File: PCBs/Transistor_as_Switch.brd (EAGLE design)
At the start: 24.2 x 19 mm, 7 parts, among them T1 2N3904

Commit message: Updated
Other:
- board size 24.2 x 19 mm -> 30 x 20 mm
- board text added: "PinwheelRobotics"
- board text added: "care@pinwheel.in"
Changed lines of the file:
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@@
 <drawing>
 <settings>
-<setting alwaysvectorfont="yes"/>
+<setting alwaysvectorfont="no"/>
 <setting verticaltext="up"/>
 </settings>
-<grid distance="50" unitdist="mil" unit="mm" style="lines" multiple="1" display="yes" altdistance="5" altunitdist="mil" altunit="mm"/>
+<grid distance="0.5" unitdist="mm" unit="mm" style="lines" multiple="1" display="yes" altdistance="5" altunitdist="mil" altunit="mm"/>
 <layers>
 <layer number="1" name="Top" color="4" fill="1" visible="yes" active="yes"/>
@@
 <layer number="43" name="vRestrict" color="2" fill="10" visible="yes" active="yes"/>
 <layer number="44" name="Drills" color="7" fill="1" visible="no" active="yes"/>
-<layer number="45" name="Holes" color="7" fill="1" visible="no" active="yes"/>
+<layer number="45" name="Holes" color="7" fill="1" visible="yes" active="yes"/>
 <layer number="46" name="Milling" color="3" fill="1" visible="no" active="yes"/>
 <layer number="47" name="Measures" color="7" fill="1" visible="no" active="yes"/>
@@
 <board>
 <plain>
-<wire x1="0" y1="17.77" x2="0" y2="1.27" width="0" layer="20"/>
-<wire x1="0" y1="1.27" x2="1.27" y2="0" width="0" layer="20" curve="90"/>
-<wire x1="1.27" y1="0" x2="22.86" y2="0" width="0" layer="20"/>
-<wire x1="22.86" y1="0" x2="24.181" y2="1.321" width="0" layer="20" curve="90"/>
-<wire x1="24.181" y1="1.321" x2="24.181" y2="17.719" width="0" layer="20"/>
-<wire x1="24.181" y1="17.719" x2="22.86" y2="19.04" width="0" layer="20" curve="90"/>
-<wire x1="22.86" y1="19.04" x2="1.27" y2="19.04" width="0" layer="20"/>
-<wire x1="1.27" y1="19.04" x2="0" y2="17.77" width="0" layer="20" curve="90"/>
+<wire x1="24.612559375" y1="20" x2="-1.0266875" y2="20" width="0.1524" layer="20"/>
+<wire x1="-1.0266875" y1="20" x2="-3" y2="18.0266875" width="0.1524" layer="20" curve="90"/>
+<wire x1="-3" y1="18.0266875" x2="-3" y2="1.197415625" width="0.1524" layer="20"/>
+<wire x1="-3" y1="1.197415625" x2="-1.802584375" y2="0" width="0.1524" layer="20" curve="90"/>
+<wire x1="-1.802584375" y1="0" x2="25.654259375" y2="0" width="0.1524" layer="20"/>
+<wire x1="25.654259375" y1="0" x2="27" y2="1.345740625" width="0.1524" layer="20" curve="90"/>
+<wire x1="27" y1="1.345740625" x2="27" y2="17.612559375" width="0.1524" layer="20"/>
+<wire x1="27" y1="17.612559375" x2="24.612559375" y2="20" width="0.1524" layer="20" curve="90"/>
+<hole x="-0.889" y="17.907" drill="3"/>
+<hole x="24.992" y="17.357" drill="3"/>
+<hole x="24.992" y="1.992" drill="3"/>
+<hole x="-0.984" y="2.119" drill="3"/>
+<text x="4.191" y="18.288" size="1.4224" layer="21">PinwheelRobotics</text>
+<text x="5.461" y="11.811" size="1.27" layer="22" rot="MR180">care@pinwheel.in</text>
 </plain>
 <attributes>

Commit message: New Update
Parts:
- moved INPUT 0.52 mm to (19.3, 7.11)
- moved OUTPUT 0.28 mm to (11.8, 7.11)
- moved GND 0.18 mm to (4.32, 7.11)
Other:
- board size 30 x 20 mm -> 29.5 x 20 mm
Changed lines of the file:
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@@
 <drawing>
 <settings>
-<setting alwaysvectorfont="no"/>
+<setting alwaysvectorfont="yes"/>
 <setting verticaltext="up"/>
 </settings>
@@
 <board>
 <plain>
-<wire x1="24.612559375" y1="20" x2="-1.0266875" y2="20" width="0.1524" layer="20"/>
+<wire x1="-1.0266875" y1="20" x2="24.792896875" y2="20" width="0.1524" layer="20"/>
+<wire x1="24.792896875" y1="20" x2="26.5" y2="18.292896875" width="0.1524" layer="20" curve="-90"/>
+<wire x1="26.5" y1="18.292896875" x2="26.5" y2="0.845740625" width="0.1524" layer="20"/>
+<wire x1="26.5" y1="0.845740625" x2="25.654259375" y2="0" width="0.1524" layer="20" curve="-90"/>
 <wire x1="-1.0266875" y1="20" x2="-3" y2="18.0266875" width="0.1524" layer="20" curve="90"/>
 <wire x1="-3" y1="18.0266875" x2="-3" y2="1.197415625" width="0.1524" layer="20"/>
 <wire x1="-3" y1="1.197415625" x2="-1.802584375" y2="0" width="0.1524" layer="20" curve="90"/>
-<wire x1="-1.802584375" y1="0" x2="25.654259375" y2="0" width="0.1524" layer="20"/>
-<wire x1="25.654259375" y1="0" x2="27" y2="1.345740625" width="0.1524" layer="20" curve="90"/>
-<wire x1="27" y1="1.345740625" x2="27" y2="17.612559375" width="0.1524" layer="20"/>
-<wire x1="27" y1="17.612559375" x2="24.612559375" y2="20" width="0.1524" layer="20" curve="90"/>
-<hole x="-0.889" y="17.907" drill="3"/>
-<hole x="24.992" y="17.357" drill="3"/>
-<hole x="24.992" y="1.992" drill="3"/>
-<hole x="-0.984" y="2.119" drill="3"/>
+<wire x1="-1.802584375" y1="0" x2="25.5" y2="0" width="0.1524" layer="20"/>
+<hole x="-1" y="17.5" drill="3"/>
+<hole x="24.5" y="17.5" drill="3"/>
+<hole x="24.5" y="2" drill="3"/>
+<hole x="-1" y="2" drill="3"/>
 <text x="4.191" y="18.288" size="1.4224" layer="21">PinwheelRobotics</text>
 <text x="5.461" y="11.811" size="1.27" layer="22" rot="MR180">care@pinwheel.in</text>
+<wire x1="25.5" y1="0" x2="25.654259375" y2="0" width="0.1524" layer="20"/>
 </plain>
 <attributes>
@@
 </autorouter>
 <elements>
-<element name="GND" library="microbit" package="MICROBIT_PAD" value="MICROBIT_PAD" x="4.445" y="6.985" smashed="yes">
-<attribute name="NAME" x="2.794" y="10.414" size="0.6096" layer="21" font="vector"/>
-</element>
-<element name="INPUT" library="microbit" package="MICROBIT_PAD" value="MICROBIT_PAD" x="19.812" y="6.985" smashed="yes">
-<attribute name="NAME" x="17.399" y="10.033" size="0.6096" layer="21" font="vector"/>
+<element name="GND" library="microbit" package="MICROBIT_PAD" value="MICROBIT_PAD" x="4.318" y="7.112" smashed="yes">
+<attribute name="NAME" x="2.667" y="10.541" size="0.6096" layer="21" font="vector"/>
+</element>
+<element name="INPUT" library="microbit" package="MICROBIT_PAD" value="MICROBIT_PAD" x="19.304" y="7.112" smashed="yes">
+<attribute name="NAME" x="16.891" y="10.16" size="0.6096" layer="21" font="vector"/>
 </element>
 <element name="LED1" library="led" library_urn="urn:adsk.eagle:library:259" package="CHIP-LED0805" package3d_urn="urn:adsk.eagle:package:15818/2" value="" x="8.255" y="16.637" smashed="yes" rot="R90">
@@
 <attribute name="VALUE" x="9.525" y="19.177" size="1.27" layer="27" rot="R180"/>
 </element>
-<element name="OUTPUT" library="microbit" package="MICROBIT_PAD" value="MICROBIT_PAD" x="12.065" y="6.985" smashed="yes">
-<attribute name="NAME" x="8.89" y="10.414" size="0.6096" layer="21" font="vector"/>
+<element name="OUTPUT" library="microbit" package="MICROBIT_PAD" value="MICROBIT_PAD" x="11.811" y="7.112" smashed="yes">
+<attribute name="NAME" x="8.636" y="10.541" size="0.6096" layer="21" font="vector"/>
 </element>
 <element name="R1" library="we-rcl" package="R0207/10" value="" x="16.002" y="13.335" smashed="yes" rot="R180">
@@
 <wire x1="21.0693" y1="13.335" x2="21.002" y2="13.335" width="0.381" layer="1"/>
 <wire x1="21.0693" y1="16.5354" x2="21.002" y2="16.637" width="0.381" layer="1"/>
-<wire x1="20.8026" y1="8.001" x2="20.8026" y2="13.335" width="0.381" layer="1"/>
-<wire x1="20.0025" y1="7.2009" x2="20.8026" y2="8.001" width="0.381" layer="1"/>
+<wire x1="20.8026" y1="8.43429375" x2="20.8026" y2="13.335" width="0.381" layer="1"/>
 <wire x1="20.8026" y1="13.335" x2="21.002" y2="13.335" width="0.381" layer="1"/>
-<wire x1="20.0025" y1="7.2009" x2="19.812" y2="6.985" width="0.381" layer="1"/>
+<wire x1="20.8026" y1="8.43429375" x2="19.304" y2="7.112" width="0.381" layer="1"/>
 </signal>
 <signal name="N$1">
@@
 <wire x1="4.0005" y1="14.1351" x2="3.81" y2="13.97" width="0.381" layer="1"/>
 <wire x1="5.334" y1="13.8684" x2="4.0005" y2="13.8684" width="0.381" layer="1"/>
-<wire x1="12.0015" y1="7.2009" x2="5.334" y2="13.8684" width="0.381" layer="1"/>
+<wire x1="11.694584375" y1="7.507815625" x2="5.334" y2="13.8684" width="0.381" layer="1"/>
 <wire x1="4.0005" y1="13.8684" x2="3.81" y2="13.97" width="0.381" layer="1"/>
-<wire x1="12.0015" y1="7.2009" x2="12.065" y2="6.985" width="0.381" layer="1"/>
+<wire x1="11.694584375" y1="7.507815625" x2="11.811" y2="7.112" width="0.381" layer="1"/>
 </signal>
 <signal name="GND">
@@
 <wire x1="4.5339" y1="7.2009" x2="5.0673" y2="7.7343" width="0.381" layer="16"/>
 <wire x1="4.0005" y1="16.2687" x2="3.81" y2="16.51" width="0.381" layer="16"/>
-<wire x1="4.5339" y1="7.2009" x2="4.445" y2="6.985" width="0.381" layer="16"/>
+<wire x1="4.5339" y1="7.2009" x2="4.318" y2="7.112" width="0.381" layer="16"/>
 </signal>
 <signal name="N$3">

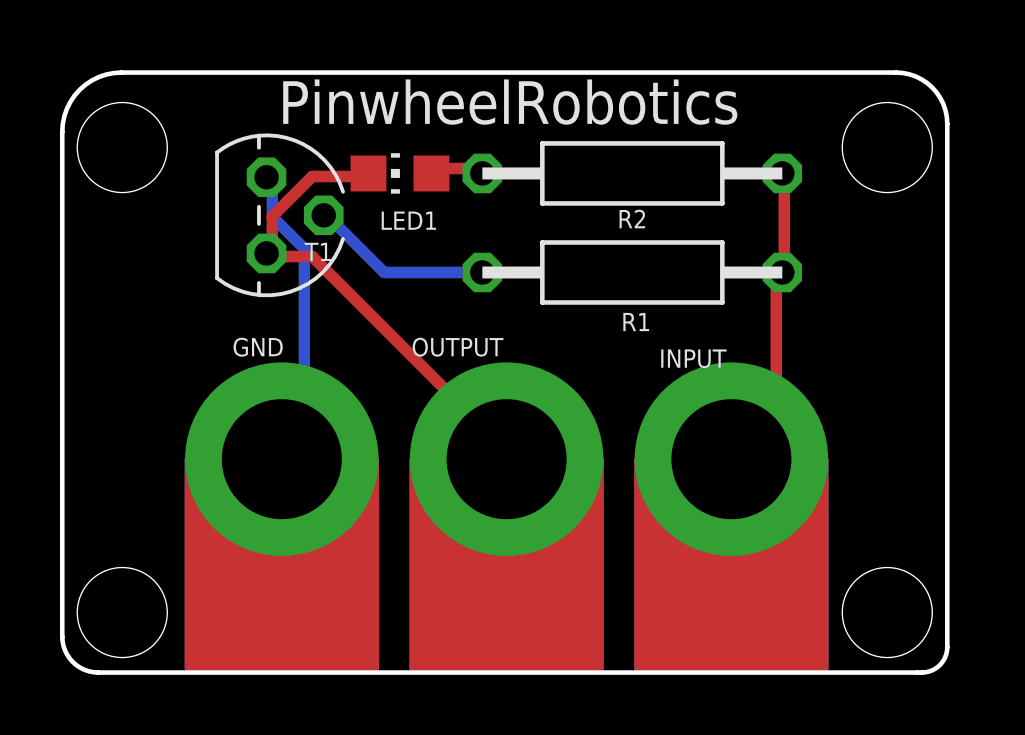
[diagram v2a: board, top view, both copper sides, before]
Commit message: New Update for board curv
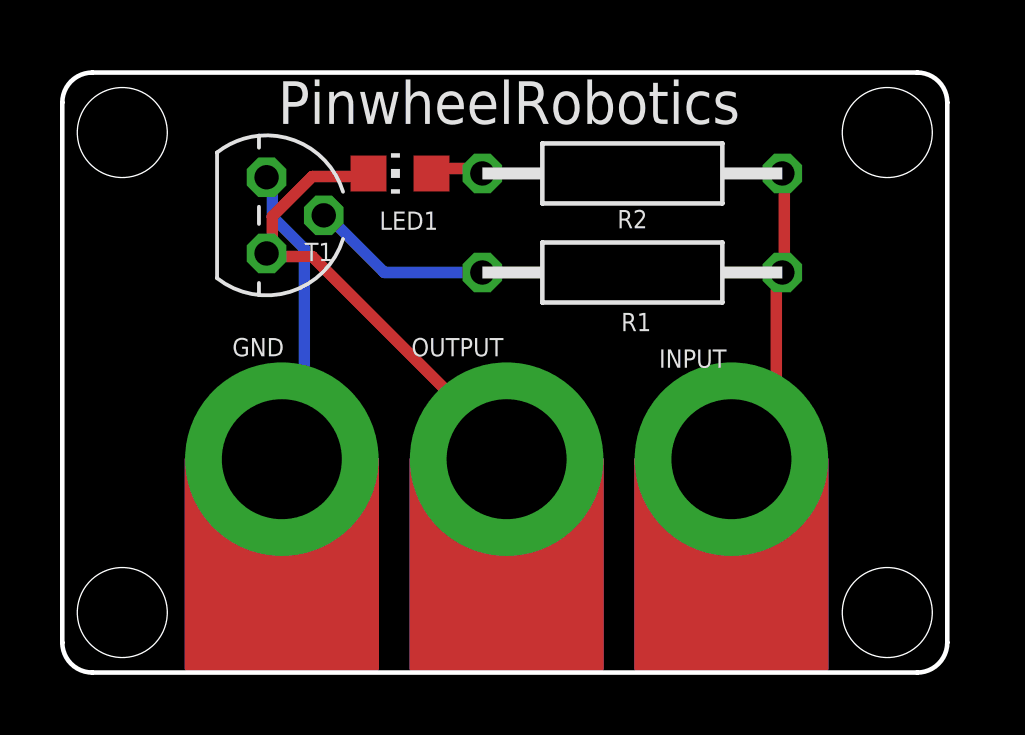
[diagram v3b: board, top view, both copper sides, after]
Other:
- outline, holes or cut-outs redrawn
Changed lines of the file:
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@@
 <board>
 <plain>
-<wire x1="-1.0266875" y1="20" x2="24.792896875" y2="20" width="0.1524" layer="20"/>
-<wire x1="24.792896875" y1="20" x2="26.5" y2="18.292896875" width="0.1524" layer="20" curve="-90"/>
-<wire x1="26.5" y1="18.292896875" x2="26.5" y2="0.845740625" width="0.1524" layer="20"/>
-<wire x1="26.5" y1="0.845740625" x2="25.654259375" y2="0" width="0.1524" layer="20" curve="-90"/>
-<wire x1="-1.0266875" y1="20" x2="-3" y2="18.0266875" width="0.1524" layer="20" curve="90"/>
-<wire x1="-3" y1="18.0266875" x2="-3" y2="1.197415625" width="0.1524" layer="20"/>
-<wire x1="-3" y1="1.197415625" x2="-1.802584375" y2="0" width="0.1524" layer="20" curve="90"/>
-<wire x1="-1.802584375" y1="0" x2="25.5" y2="0" width="0.1524" layer="20"/>
-<hole x="-1" y="17.5" drill="3"/>
-<hole x="24.5" y="17.5" drill="3"/>
+<wire x1="25.5" y1="0" x2="26.5" y2="1" width="0.1524" layer="20" curve="90"/>
+<wire x1="26.5" y1="1" x2="26.5" y2="19" width="0.1524" layer="20"/>
+<wire x1="26.5" y1="19" x2="25.5" y2="20" width="0.1524" layer="20" curve="90"/>
+<wire x1="25.5" y1="20" x2="-2" y2="20" width="0.1524" layer="20"/>
+<wire x1="-2" y1="20" x2="-3" y2="19" width="0.1524" layer="20" curve="90"/>
+<wire x1="-3" y1="19" x2="-3" y2="1" width="0.1524" layer="20"/>
+<wire x1="-3" y1="1" x2="-2" y2="0" width="0.1524" layer="20" curve="90"/>
+<wire x1="-2" y1="0" x2="25.5" y2="0" width="0.1524" layer="20"/>
+<hole x="-1" y="18" drill="3"/>
+<hole x="24.5" y="18" drill="3"/>
 <hole x="24.5" y="2" drill="3"/>
 <hole x="-1" y="2" drill="3"/>
 <text x="4.191" y="18.288" size="1.4224" layer="21">PinwheelRobotics</text>
 <text x="5.461" y="11.811" size="1.27" layer="22" rot="MR180">care@pinwheel.in</text>
-<wire x1="25.5" y1="0" x2="25.654259375" y2="0" width="0.1524" layer="20"/>
 </plain>
 <attributes>

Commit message: Dimension added
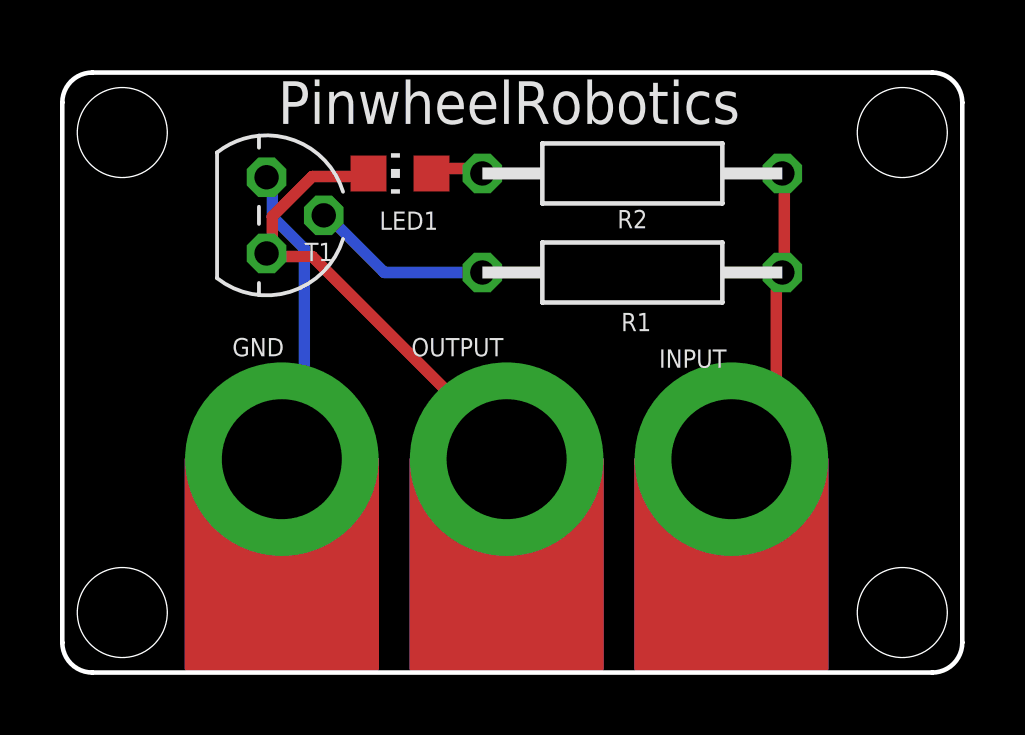
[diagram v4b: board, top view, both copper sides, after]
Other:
- board size 29.5 x 20 mm -> 30 x 20 mm
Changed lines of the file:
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@@
 <drawing>
 <settings>
-<setting alwaysvectorfont="yes"/>
+<setting alwaysvectorfont="no"/>
 <setting verticaltext="up"/>
 </settings>
@@
 <board>
 <plain>
-<wire x1="25.5" y1="0" x2="26.5" y2="1" width="0.1524" layer="20" curve="90"/>
-<wire x1="26.5" y1="1" x2="26.5" y2="19" width="0.1524" layer="20"/>
-<wire x1="26.5" y1="19" x2="25.5" y2="20" width="0.1524" layer="20" curve="90"/>
-<wire x1="25.5" y1="20" x2="-2" y2="20" width="0.1524" layer="20"/>
-<wire x1="-2" y1="20" x2="-3" y2="19" width="0.1524" layer="20" curve="90"/>
 <wire x1="-3" y1="19" x2="-3" y2="1" width="0.1524" layer="20"/>
 <wire x1="-3" y1="1" x2="-2" y2="0" width="0.1524" layer="20" curve="90"/>
-<wire x1="-2" y1="0" x2="25.5" y2="0" width="0.1524" layer="20"/>
+<wire x1="-2" y1="0" x2="26" y2="0" width="0.1524" layer="20"/>
+<wire x1="26" y1="0" x2="27" y2="1" width="0.1524" layer="20" curve="90"/>
+<wire x1="27" y1="1" x2="27" y2="19" width="0.1524" layer="20"/>
+<wire x1="27" y1="19" x2="26" y2="20" width="0.1524" layer="20" curve="90"/>
+<wire x1="26" y1="20" x2="-2" y2="20" width="0.1524" layer="20"/>
+<wire x1="-2" y1="20" x2="-3" y2="19" width="0.1524" layer="20" curve="90"/>
 <hole x="-1" y="18" drill="3"/>
-<hole x="24.5" y="18" drill="3"/>
-<hole x="24.5" y="2" drill="3"/>
+<hole x="25" y="18" drill="3"/>
+<hole x="25" y="2" drill="3"/>
 <hole x="-1" y="2" drill="3"/>
 <text x="4.191" y="18.288" size="1.4224" layer="21">PinwheelRobotics</text>
